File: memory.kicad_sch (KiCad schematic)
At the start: 0 parts

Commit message: Added EEProm
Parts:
- added U1: M24C64-WMN6TP, M24C64-WMN6TP:SOIC127P600X175-8N, symbol M24C64-WMN6TP:M24C64-WMN6TP
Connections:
- new net +3.3V: U1.8 (VCC)
- new net GND: U1.1 (E0), U1.2 (E1), U1.3 (E2), U1.4 (VSS)
- new net GPIO_!WC: U1.7 (~{WC})
- new net I2C1_SCL: U1.6 (SCL)
- new net I2C1_SDA: U1.5 (SDA)

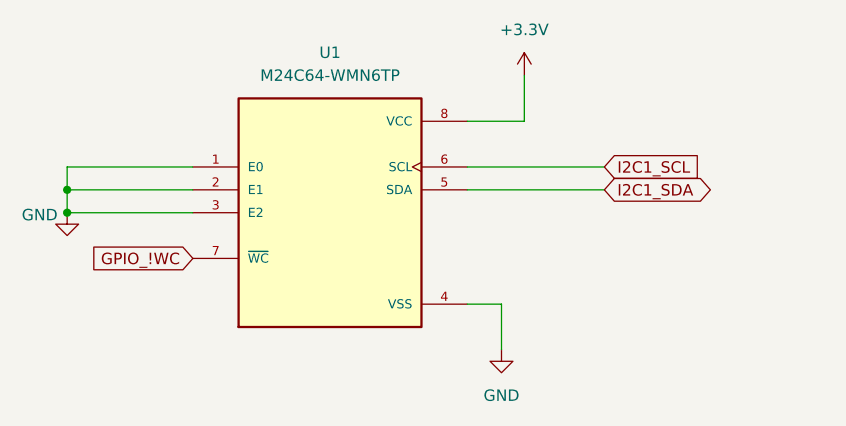
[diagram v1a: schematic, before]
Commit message: Added Pull-Up Resistors to EEProm I2C pins
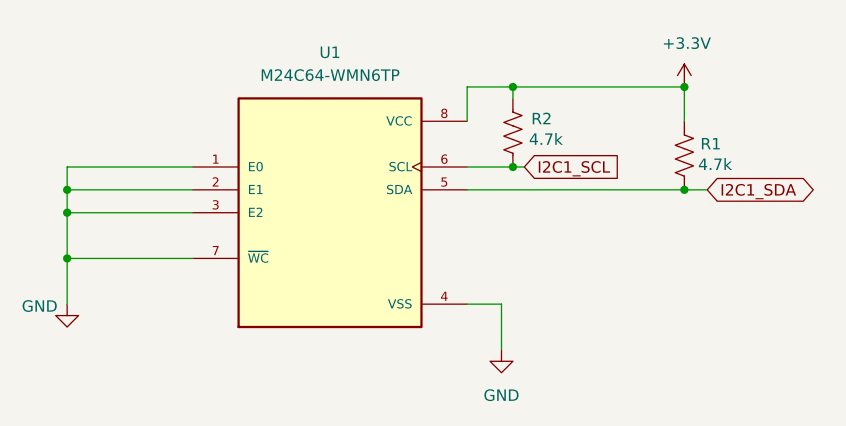
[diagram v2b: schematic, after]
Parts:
- added R1, R2: 4.7k, symbol Device:R_US
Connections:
- net GPIO_!WC is gone; now on net GND: U1.7 (~{WC})
- net +3.3V: now also R1.1, R2.1
- net I2C1_SCL: now also R2.2
- net I2C1_SDA: now also R1.2

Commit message: added MCU decaps and hall effect schematic
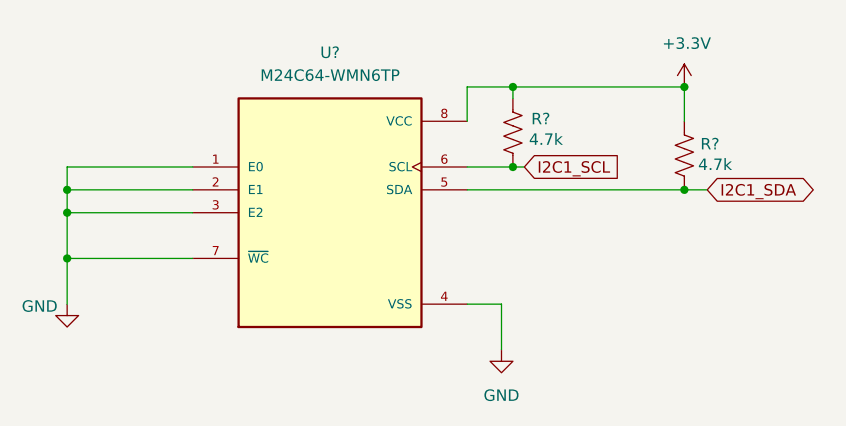
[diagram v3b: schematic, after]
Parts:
- renumbered R2 to R?, R1 to R?, U1 to U?
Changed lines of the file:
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@@
 		(on_board yes)
 		(dnp no)
-		(property "Reference" "#PWR03"
+		(property "Reference" "#PWR?"
 			(at 182.88 90.17 0)
 			(effects
@@
 		)
 		(instances
+			(project "senior_design"
+				(path "/35c074f0-8545-4dc1-a57d-3ef0bc7d9188/97e7f441-78af-47c4-8e49-e87c6db6b63d"
+					(reference "#PWR?")
+					(unit 1)
+				)
+			)
 			(project "memory"
 				(path "/ea50c2bc-1de0-48a1-af67-17bbf96ee86d"
@@
 		(on_board yes)
 		(dnp no)
-		(property "Reference" "R2"
+		(property "Reference" "R?"
 			(at 165.862 89.916 0)
 			(effects
@@
 		)
 		(instances
+			(project "senior_design"
+				(path "/35c074f0-8545-4dc1-a57d-3ef0bc7d9188/97e7f441-78af-47c4-8e49-e87c6db6b63d"
+					(reference "R?")
+					(unit 1)
+				)
+			)
 			(project "memory"
 				(path "/ea50c2bc-1de0-48a1-af67-17bbf96ee86d"
@@
 		(dnp no)
 		(fields_autoplaced yes)
-		(property "Reference" "U1"
+		(property "Reference" "U?"
 			(at 143.51 82.55 0)
 			(effects
@@
 		)
 		(instances
+			(project "senior_design"
+				(path "/35c074f0-8545-4dc1-a57d-3ef0bc7d9188/97e7f441-78af-47c4-8e49-e87c6db6b63d"
+					(reference "U?")
+					(unit 1)
+				)
+			)
 			(project "memory"
 				(path "/ea50c2bc-1de0-48a1-af67-17bbf96ee86d"
@@
 		(dnp no)
 		(fields_autoplaced yes)
-		(property "Reference" "#PWR02"
+		(property "Reference" "#PWR?"
 			(at 162.56 121.92 0)
 			(effects
@@
 		)
 		(instances
+			(project "senior_design"
+				(path "/35c074f0-8545-4dc1-a57d-3ef0bc7d9188/97e7f441-78af-47c4-8e49-e87c6db6b63d"
+					(reference "#PWR?")
+					(unit 1)
+				)
+			)
 			(project "memory"
 				(path "/ea50c2bc-1de0-48a1-af67-17bbf96ee86d"
@@
 		(on_board yes)
 		(dnp no)
-		(property "Reference" "R1"
+		(property "Reference" "R?"
 			(at 184.658 92.71 0)
 			(effects
@@
 		)
 		(instances
+			(project "senior_design"
+				(path "/35c074f0-8545-4dc1-a57d-3ef0bc7d9188/97e7f441-78af-47c4-8e49-e87c6db6b63d"
+					(reference "R?")
+					(unit 1)
+				)
+			)
 			(project "memory"
 				(path "/ea50c2bc-1de0-48a1-af67-17bbf96ee86d"
@@
 		(on_board yes)
 		(dnp no)
-		(property "Reference" "#PWR01"
+		(property "Reference" "#PWR?"
 			(at 114.3 116.84 0)
 			(effects
@@
 		)
 		(instances
-			(project "memory"
-				(path "/ea50c2bc-1de0-48a1-af67-17bbf96ee86d"
+			(project "senior_design"
+				(path "/35c074f0-8545-4dc1-a57d-3ef0bc7d9188/97e7f441-78af-47c4-8e49-e87c6db6b63d"
+					(reference "#PWR?")
+					(unit 1)
+				)
+			)
+			(project "memory"
+				(path "/ea50c2bc-1de0-48a1-af67-17bbf96ee86d"

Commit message: Added footprint library for EEProm
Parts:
- U?: footprint M24C64-WMN6TP:SOIC127P600X175-8N -> EEProm Footprint:SOIC127P600X175-8N
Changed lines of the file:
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@@
 			)
 		)
-		(property "Footprint" "M24C64-WMN6TP:SOIC127P600X175-8N"
+		(property "Footprint" "EEProm Footprint:SOIC127P600X175-8N"
 			(at 143.51 100.33 0)
 			(effects
